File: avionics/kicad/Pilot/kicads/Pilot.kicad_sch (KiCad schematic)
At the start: 120 parts, among them X2Y-CAN 4.7nF X2Y, X2Y-RS485 4.7nF X2Y

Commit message: Pilot: move PB2 rails to 4.80 mm on male TSM-DV-LC strips and re-floor-plan (WBS R2)
The Pilot generator still had the unsourced 2.54 mm rail rows (29.92 mm
apart) and female socket footprints, so the cape could not mate with the
PB2-I. Same correction TACCO received on 2026-10-05:

- Rails at v 4.80 / 30.20 (PB2 SRM Fig. 3.45), Samtec TSM-118-04-L-DV-LC
  male SMT strips; -LC clip NPTHs at +/-20.32 mm.
- Bottom-face height budget (~5.54 mm stack, PB2-I microSD / JST-SH
  obstructions): both 8.9 mm Ethernet transformers to the top face, 1553
  transformer between the band and the JST-SH, GPS to B.Cu.
- TACCO-style isolation band: isolators on F.Cu at v 20.6, bus connectors
  at the bottom edge over the P2 rail, ISO_BAND on F.Cu + inner layers;
  only two-pad parts, GPS and 1553-XFM on B.Cu beneath it.
- J-PWM shifted 1.6 mm so its pad-1 column clears the P1 clip hole.

Gates: ERC 0 errors (10 accepted lib_symbol_issues), DRC 0 with schematic
parity 0, 120/120 placed, bottom-face height/under-band audit 0 violations.
Routing remains open.

Co-Authored-By: Claude Opus 5.5 <noreply@anthropic.com>
Claude-Session: https://claude.ai/code/session_01YLwDy53g1VCBzNBwW4moUC
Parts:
- PB2-P1: footprint Serenity-Custom:PocketBeagle2_2x18_P1_Socket -> Serenity-Custom:PocketBeagle2_2x18_P1_TSM-DV-LC; MPN (none) -> TSM-118-04-L-DV-LC
- PB2-P2: footprint Serenity-Custom:PocketBeagle2_2x18_P2_Socket -> Serenity-Custom:PocketBeagle2_2x18_P2_TSM-DV-LC; MPN (none) -> TSM-118-04-L-DV-LC
- TVS-CAN: footprint Package_TO_SOT_SMD:SOT-143 -> Package_TO_SOT_SMD:SOT-363_SC-70-6; symbol SecureControllers:PRTR5V0U2X -> Pilot:S_TVS-CAN
- TVS-RS485: footprint Package_TO_SOT_SMD:SOT-143 -> Package_TO_SOT_SMD:SOT-363_SC-70-6; symbol SecureControllers:PRTR5V0U2X -> Pilot:S_TVS-RS485
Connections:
- net CAN_H_F: now also TVS-CAN.1 (IO1); no longer TVS-CAN.2 (IO1)
- net GND2_CAN: now also TVS-CAN.2 (GND); no longer TVS-CAN.1 (GND)
- net GND2_RS485: now also TVS-RS485.2 (GND); no longer TVS-RS485.1 (GND)
- net RS485_A_F: now also TVS-RS485.1 (IO1); no longer TVS-RS485.2 (IO1)
- net VCC2_CAN: now also TVS-CAN.5 (VCC); no longer TVS-CAN.4 (VCC)
- net VCC2_RS485: now also TVS-RS485.5 (VCC); no longer TVS-RS485.4 (VCC)
- no-connect marks 87 -> 91
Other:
- note removed: "WÜRTH ELEKTRONIK USAGE NOTICE (verbatim, 749010012A data sheet rev 004.000 p.1; applies to Würth parts on this board: 749010012A, 742792512, WE-MAPI 3015): This electronic component has been designed and developed for usage in general electronic equipment only. This product is not authorized for use in equipment where a higher safety standard and reliability standard is especially required or whe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"

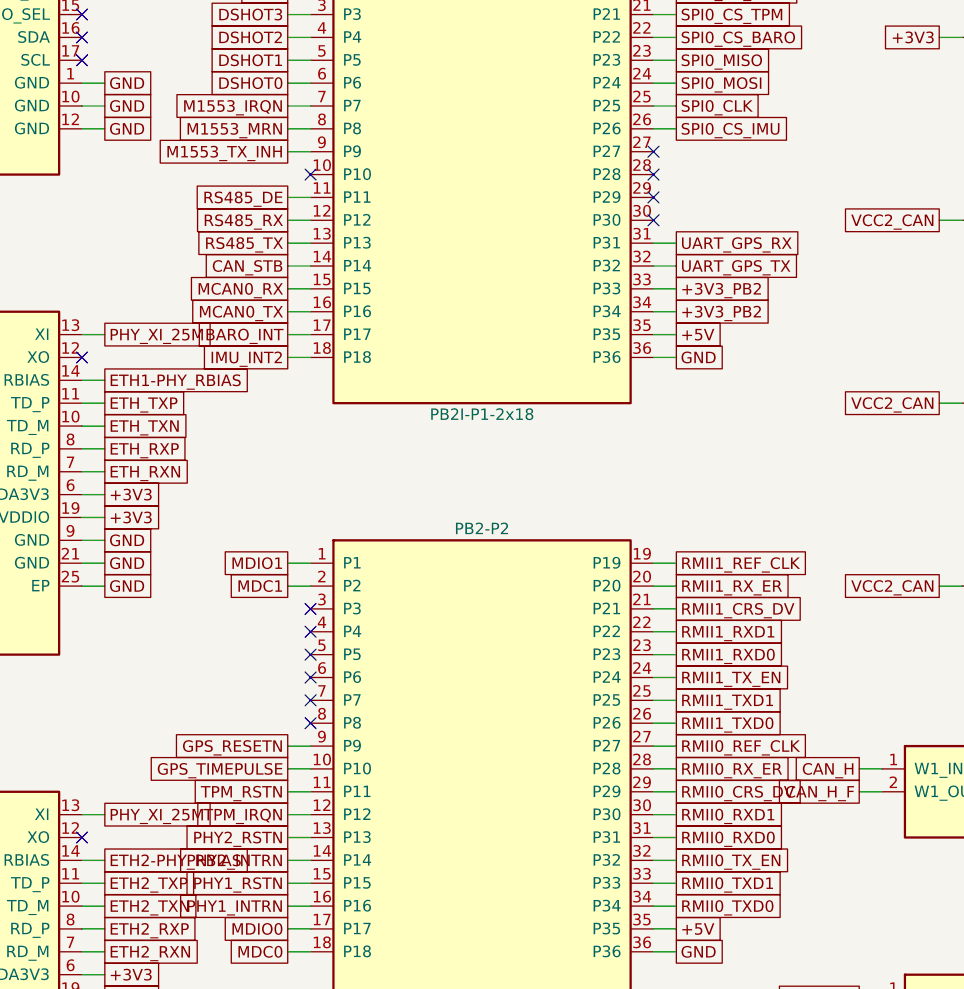
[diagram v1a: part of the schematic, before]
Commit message: Pilot: move TPM_RSTN/TPM_IRQN from PB2 P2-11/12 to P1-28/29 (ideation idea 10)
TPM sits over the P1 rail; P2-11/12 were 26-31 mm away and inside ISO_BAND
(no legal via). New pins P1-28 GPIO0_43 / P1-29 GPIO0_62 are 6-7 mm from TPM
pins 17/18, per PocketBeagle 2 SRM sec 4.2 mux tables. P1-27 (AIN4) and
P1-30 (UART0_TXD console) rejected.

- gen_pilot_sch.py pin map edited; generator verified byte-identical to the
  committed schematic before the edit; ERC 0 before and after.
- Pilot.net re-exported; PCB pad nets edited in place (owner hand placement
  preserved): DRC 0 errors, parity 0, 136 unconnected (unchanged; both nets
  were already unrouted, now short).
- Idea 11 (clock HI-6138 from PHY 50MHzOut, delete X-50M) NOT done: contradicts
  the recorded decision that a PHY reset must not stop 1553, and needs a
  22-23 mm 50 MHz branch vs the current 1.6 mm oscillator trace.

Co-Authored-By: Claude Opus 5.5 (1M context) <noreply@anthropic.com>
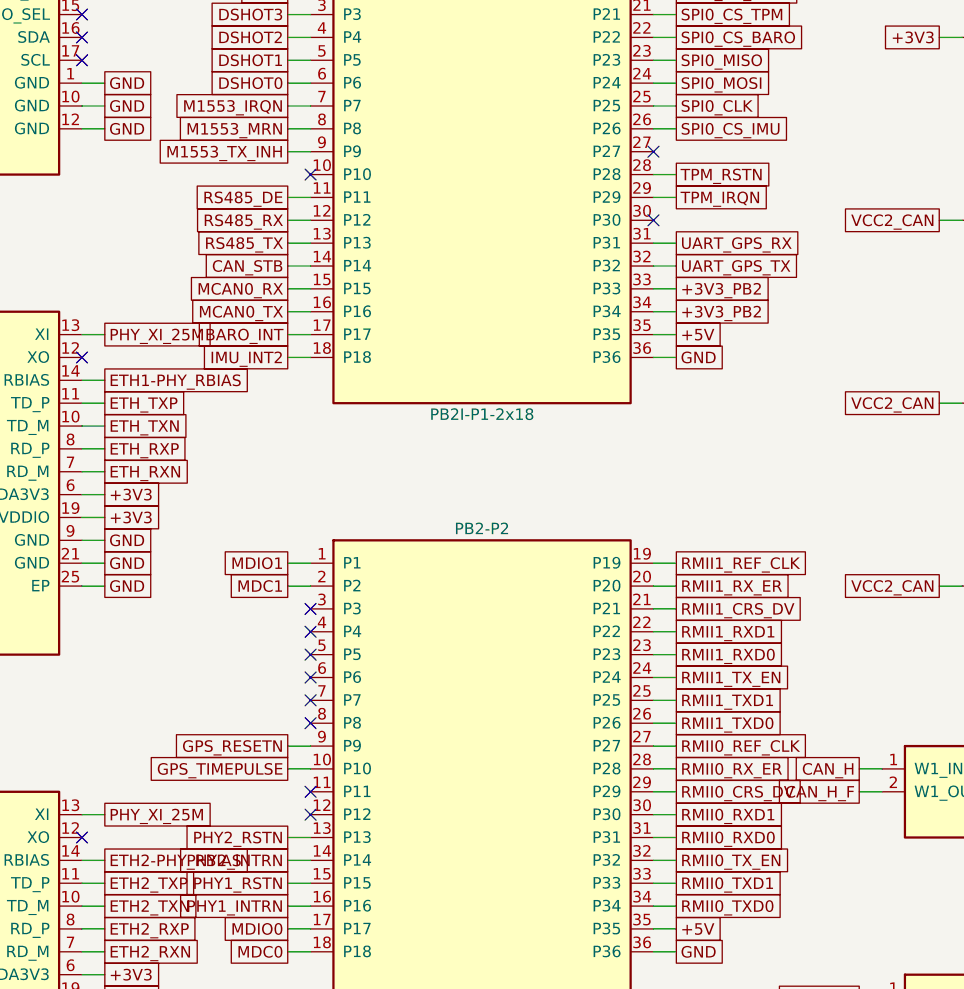
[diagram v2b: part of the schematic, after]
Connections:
- net TPM_IRQN: now also PB2-P1.29 (P29); no longer PB2-P2.12 (P12)
- net TPM_RSTN: now also PB2-P1.28 (P28); no longer PB2-P2.11 (P11)
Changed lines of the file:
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@@
   (global_label "SPI0_CS_IMU" (shape passive) (at 161.29 271.78 0) (effects (font (size 1.27 1.27)) (justify left)))
   (no_connect (at 158.75 274.32))
-  (no_connect (at 158.75 276.86))
-  (no_connect (at 158.75 279.40))
+  (wire (pts (xy 158.75 276.86) (xy 161.29 276.86)) (stroke (width 0) (type default)))
+  (global_label "TPM_RSTN" (shape passive) (at 161.29 276.86 0) (effects (font (size 1.27 1.27)) (justify left)))
+  (wire (pts (xy 158.75 279.40) (xy 161.29 279.40)) (stroke (width 0) (type default)))
+  (global_label "TPM_IRQN" (shape passive) (at 161.29 279.40 0) (effects (font (size 1.27 1.27)) (justify left)))
   (no_connect (at 158.75 281.94))
   (wire (pts (xy 158.75 284.48) (xy 161.29 284.48)) (stroke (width 0) (type default)))
@@
   (wire (pts (xy 120.65 342.90) (xy 118.11 342.90)) (stroke (width 0) (type default)))
   (global_label "GPS_TIMEPULSE" (shape passive) (at 118.11 342.90 180) (effects (font (size 1.27 1.27)) (justify right)))
-  (wire (pts (xy 120.65 345.44) (xy 118.11 345.44)) (stroke (width 0) (type default)))
-  (global_label "TPM_RSTN" (shape passive) (at 118.11 345.44 180) (effects (font (size 1.27 1.27)) (justify right)))
-  (wire (pts (xy 120.65 347.98) (xy 118.11 347.98)) (stroke (width 0) (type default)))
-  (global_label "TPM_IRQN" (shape passive) (at 118.11 347.98 180) (effects (font (size 1.27 1.27)) (justify right)))
+  (no_connect (at 120.65 345.44))
+  (no_connect (at 120.65 347.98))
   (wire (pts (xy 120.65 350.52) (xy 118.11 350.52)) (stroke (width 0) (type default)))
   (global_label "PHY2_RSTN" (shape passive) (at 118.11 350.52 180) (effects (font (size 1.27 1.27)) (justify right)))

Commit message: Pilot sch: ISOW §13.1 ferrite beads + split DC-DC output nets (ERC 0)
Owner decision 2026-10-12: treat ISOW1044 SLLSFF7A §13.1 [REF-SENSOR-009] and
ISOW1412 SLLSF86C §13.1 [REF-SENSOR-010] as binding.

- New nets VCC2_CAN_DCDC / GND2_CAN_DCDC / VCC2_RS485_DCDC / GND2_RS485_DCDC
  on VISOOUT (12, + VSIN 13 on ISOW1044) and GND2 (11); ISOW1412 MODE (13)
  tied to GND2 per §13.1.
- Four BLM15EX331SN1D beads (FB-CAN-V/G, FB-485-V/G) between VISOOUT->VISOIN
  and GND2->GISOIN (§13.1 item 4) [REF-SENSOR-043, new].
- C-CAN4 / C-485-4 10 nF HF caps 0201 -> 0402 on the DC-DC side (item 2);
  bulk C-CAN5 / C-485-5 on the DC-DC side (item 3).
- 124 parts, 599 pins, ERC 0; netlist re-exported.  PCB not yet updated.

Co-Authored-By: Claude Opus 5.5 (1M context) <noreply@anthropic.com>
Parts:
- removed C-1553A: 100nF, Capacitor_SMD:C_0402_1005Metric, symbol Pilot:S_C-1553A
- removed C-1553B: 100nF, Capacitor_SMD:C_0402_1005Metric, symbol Pilot:S_C-1553B
- removed C-25M: 100nF, Capacitor_SMD:C_0402_1005Metric, symbol Pilot:S_C-25M
- removed C-485-1: 10nF, Capacitor_SMD:C_0201_0603Metric, symbol Pilot:S_C-485-1
- removed C-485-2: 10uF 10V X5R, Capacitor_SMD:C_0805_2012Metric, symbol Pilot:S_C-485-2
- removed C-50M: 100nF, Capacitor_SMD:C_0402_1005Metric, symbol Pilot:S_C-50M
- removed C-BARO1: 100nF, Capacitor_SMD:C_0402_1005Metric, symbol Pilot:S_C-BARO1
- removed C-BS1: 10nF 2kV, Capacitor_SMD:C_1808_4520Metric, symbol Pilot:S_C-BS1
- removed C-IMU1: 100nF, Capacitor_SMD:C_0402_1005Metric, symbol Pilot:S_C-IMU1
- removed C-IMU2: 10nF, Capacitor_SMD:C_0201_0603Metric, symbol Pilot:S_C-IMU2
- removed C-P1-A1: 10nF, Capacitor_SMD:C_0201_0603Metric, symbol Pilot:S_C-P1-A1
- removed C-P1-A2: 100nF, Capacitor_SMD:C_0402_1005Metric, symbol Pilot:S_C-P1-A2
- removed R-1553P: 55R 2%, Resistor_SMD:R_0603_1608Metric, symbol Pilot:S_R-1553P
- removed R-BS1R: 75R, Resistor_SMD:R_0402_1005Metric, symbol Pilot:S_R-BS1R
- removed R-BS1T: 75R, Resistor_SMD:R_0402_1005Metric, symbol Pilot:S_R-BS1T
- removed R-P1-AD0: 2.49k, Resistor_SMD:R_0201_0603Metric, symbol Pilot:S_R-P1-AD0
- removed R-P1-RBIAS: 6.49k 1%, Resistor_SMD:R_0201_0603Metric, symbol Pilot:S_R-P1-RBIAS
- added C-485-6: 100nF, Capacitor_SMD:C_0402_1005Metric, symbol Pilot:S_C-485-6
- added C-BS2: 10nF 2kV, Capacitor_SMD:C_1808_4520Metric, symbol Pilot:S_C-BS2
- added C-CAN6: 100nF, Capacitor_SMD:C_0402_1005Metric, symbol Pilot:S_C-CAN6
- added C-P2-CRD1: 100nF, Capacitor_SMD:C_0402_1005Metric, symbol Pilot:S_C-P2-CRD1
- added C-P2-CRD2: 1uF, Capacitor_SMD:C_0402_1005Metric, symbol Pilot:S_C-P2-CRD2
- added C-P2-CTD1: 100nF, Capacitor_SMD:C_0402_1005Metric, symbol Pilot:S_C-P2-CTD1
- added C-P2-CTD2: 1uF, Capacitor_SMD:C_0402_1005Metric, symbol Pilot:S_C-P2-CTD2
- added C-TPM4: 100nF, Capacitor_SMD:C_0402_1005Metric, symbol Pilot:S_C-TPM4
- added CMC-CAN: SRF2012-100Y, Serenity-Custom:Bourns_SRF2012_4T, symbol Pilot:S_CMC-CAN
- added CMC-RS485: SRF2012-100Y, Serenity-Custom:Bourns_SRF2012_4T, symbol Pilot:S_CMC-RS485
- added FB-485-G: 330R@100MHz, Inductor_SMD:L_0402_1005Metric, symbol Pilot:S_FB-485-G
- added FB-485-V: 330R@100MHz, Inductor_SMD:L_0402_1005Metric, symbol Pilot:S_FB-485-V
- added J-PWM: TSM-108-01-L-DV, Serenity-Custom:Samtec_TSM-108-01-x-DV, symbol Pilot:S_J-PWM
- added MIL-1553: SM04B-GHS-TB, Connector_JST:JST_GH_SM04B-GHS-TB_1x04-1MP_P1.25mm_Horizontal, symbol Pilot:S_MIL-1553
- added R-1553IRQ: 10k, Resistor_SMD:R_0402_1005Metric, symbol Pilot:S_R-1553IRQ
- added R-BS2R: 75R, Resistor_SMD:R_0402_1005Metric, symbol Pilot:S_R-BS2R
- added R-TPM10: 10k, Resistor_SMD:R_0201_0603Metric, symbol Pilot:S_R-TPM10
- added R-TPMCS: 10k, Resistor_SMD:R_0201_0603Metric, symbol Pilot:S_R-TPMCS
- added TVS-1553N: SMAJ33CA, Diode_SMD:D_SMA, symbol Pilot:S_TVS-1553N
- added X-25M: 25MHz 3.3V, Oscillator:Oscillator_SMD_ECS_2520MV-xxx-xx-4Pin_2.5x2.0mm, symbol Pilot:S_X-25M
- added X-50M: 50MHz 3.3V, Oscillator:Oscillator_SMD_ECS_2520MV-xxx-xx-4Pin_2.5x2.0mm, symbol Pilot:S_X-50M
- C-1553A: renamed from R-1553IRQ; value 10k -> 100nF; footprint Resistor_SMD:R_0402_1005Metric -> Capacitor_SMD:C_0402_1005Metric; symbol Pilot:S_R-1553IRQ -> Pilot:S_C-1553A
- C-1553B: renamed from X-50M; value 50MHz 3.3V -> 100nF; footprint Oscillator:Oscillator_SMD_ECS_2520MV-xxx-xx-4Pin_2.5x2.0mm -> Capacitor_SMD:C_0402_1005Metric; symbol Pilot:S_X-50M -> Pilot:S_C-1553B; MPN ECS-2520MV-500-BN-TR -> (none)
- C-25M: renamed from TVS-1553N; value SMAJ33CA -> 100nF; footprint Diode_SMD:D_SMA -> Capacitor_SMD:C_0402_1005Metric; symbol Pilot:S_TVS-1553N -> Pilot:S_C-25M; MPN SMAJ33CA -> (none)
- C-485-1: renamed from C-485-3; value 100nF -> 10nF; footprint Capacitor_SMD:C_0402_1005Metric -> Capacitor_SMD:C_0201_0603Metric; symbol Pilot:S_C-485-3 -> Pilot:S_C-485-1
- C-485-2: renamed from C-485-4; value 10nF -> 10uF 10V X5R; footprint Capacitor_SMD:C_0201_0603Metric -> Capacitor_SMD:C_0805_2012Metric; symbol Pilot:S_C-485-4 -> Pilot:S_C-485-2
- C-485-3: renamed from C-485-5; value 10uF 10V X5R -> 100nF; footprint Capacitor_SMD:C_0805_2012Metric -> Capacitor_SMD:C_0402_1005Metric; symbol Pilot:S_C-485-5 -> Pilot:S_C-485-3
- C-485-4: renamed from C-485-6; value 100nF -> 10nF; symbol Pilot:S_C-485-6 -> Pilot:S_C-485-4
- C-485-5: renamed from CMC-RS485; value SRF2012-100Y -> 10uF 10V X5R; footprint Serenity-Custom:Bourns_SRF2012_4T -> Capacitor_SMD:C_0805_2012Metric; symbol Pilot:S_CMC-RS485 -> Pilot:S_C-485-5; MPN SRF2012-121YA -> (none)
- C-50M: renamed from C-BARO2; symbol Pilot:S_C-BARO2 -> Pilot:S_C-50M
- C-ANT: renamed from C-TPM2; value 100nF -> 10nF X7R; symbol Pilot:S_C-TPM2 -> Pilot:S_C-ANT
- C-BARO1: renamed from R-ANT; value 10R -> 100nF; footprint Resistor_SMD:R_0201_0603Metric -> Capacitor_SMD:C_0402_1005Metric; symbol Pilot:S_R-ANT -> Pilot:S_C-BARO1
- C-BARO2: renamed from C-ANT; value 10nF X7R -> 100nF; symbol Pilot:S_C-ANT -> Pilot:S_C-BARO2
- C-BS1: renamed from X-25M; value 25MHz 3.3V -> 10nF 2kV; footprint Oscillator:Oscillator_SMD_ECS_2520MV-xxx-xx-4Pin_2.5x2.0mm -> Capacitor_SMD:C_1808_4520Metric; symbol Pilot:S_X-25M -> Pilot:S_C-BS1; MPN ECS-2520MV-250-BN-TR -> (none)
- C-CAN4: footprint Capacitor_SMD:C_0201_0603Metric -> Capacitor_SMD:C_0402_1005Metric
- C-GPS1: renamed from L-ANT; value 27nH -> 10uF 6.3V X5R; footprint Inductor_SMD:L_0402_1005Metric -> Capacitor_SMD:C_0805_2012Metric; symbol Pilot:S_L-ANT -> Pilot:S_C-GPS1; MPN LQG15HN27NJ02D -> (none)
- C-GPS2: renamed from J-ANT; value U.FL-R-SMT-1 -> 100nF; footprint Connector_Coaxial:U.FL_Hirose_U.FL-R-SMT-1_Vertical -> Capacitor_SMD:C_0402_1005Metric; symbol Pilot:S_J-ANT -> Pilot:S_C-GPS2; MPN U.FL-R-SMT-1(10) -> (none)
- C-IMU1: renamed from C-GPS1; value 10uF 6.3V X5R -> 100nF; footprint Capacitor_SMD:C_0805_2012Metric -> Capacitor_SMD:C_0402_1005Metric; symbol Pilot:S_C-GPS1 -> Pilot:S_C-IMU1
- C-IMU2: renamed from C-GPS2; value 100nF -> 10nF; footprint Capacitor_SMD:C_0402_1005Metric -> Capacitor_SMD:C_0201_0603Metric; symbol Pilot:S_C-GPS2 -> Pilot:S_C-IMU2
- C-P1-A1: renamed from C-P1-IO2; value 100nF -> 10nF; footprint Capacitor_SMD:C_0402_1005Metric -> Capacitor_SMD:C_0201_0603Metric; symbol Pilot:S_C-P1-IO2 -> Pilot:S_C-P1-A1
- C-P1-A2: renamed from C-P1-IO3; value 1uF -> 100nF; symbol Pilot:S_C-P1-IO3 -> Pilot:S_C-P1-A2
- C-P1-A3: renamed from C-P1-CTD1; value 100nF -> 1uF; symbol Pilot:S_C-P1-CTD1 -> Pilot:S_C-P1-A3
- C-P1-CRD1: renamed from C-P2-A1; value 10nF -> 100nF; footprint Capacitor_SMD:C_0201_0603Metric -> Capacitor_SMD:C_0402_1005Metric; symbol Pilot:S_C-P2-A1 -> Pilot:S_C-P1-CRD1
- C-P1-CRD2: renamed from C-P2-A2; value 100nF -> 1uF; symbol Pilot:S_C-P2-A2 -> Pilot:S_C-P1-CRD2
- C-P1-CTD1: renamed from R-P2-RBIAS; value 6.49k 1% -> 100nF; footprint Resistor_SMD:R_0201_0603Metric -> Capacitor_SMD:C_0402_1005Metric; symbol Pilot:S_R-P2-RBIAS -> Pilot:S_C-P1-CTD1
- C-P1-CTD2: renamed from R-P2-AD0; value 2.49k -> 1uF; footprint Resistor_SMD:R_0201_0603Metric -> Capacitor_SMD:C_0402_1005Metric; symbol Pilot:S_R-P2-AD0 -> Pilot:S_C-P1-CTD2
- C-P1-IO1: renamed from C-P1-CTD2; value 1uF -> 10nF; footprint Capacitor_SMD:C_0402_1005Metric -> Capacitor_SMD:C_0201_0603Metric; symbol Pilot:S_C-P1-CTD2 -> Pilot:S_C-P1-IO1
- C-P1-IO2: renamed from C-P1-CRD1; symbol Pilot:S_C-P1-CRD1 -> Pilot:S_C-P1-IO2
- C-P1-IO3: renamed from C-P1-CRD2; symbol Pilot:S_C-P1-CRD2 -> Pilot:S_C-P1-IO3
- C-P2-A1: renamed from C-P2-IO2; value 100nF -> 10nF; footprint Capacitor_SMD:C_0402_1005Metric -> Capacitor_SMD:C_0201_0603Metric; symbol Pilot:S_C-P2-IO2 -> Pilot:S_C-P2-A1
- C-P2-A2: renamed from C-P2-IO3; value 1uF -> 100nF; symbol Pilot:S_C-P2-IO3 -> Pilot:S_C-P2-A2
- C-P2-A3: renamed from C-P2-CTD1; value 100nF -> 1uF; symbol Pilot:S_C-P2-CTD1 -> Pilot:S_C-P2-A3
- C-P2-IO1: renamed from C-P2-CTD2; value 1uF -> 10nF; footprint Capacitor_SMD:C_0402_1005Metric -> Capacitor_SMD:C_0201_0603Metric; symbol Pilot:S_C-P2-CTD2 -> Pilot:S_C-P2-IO1
- C-P2-IO2: renamed from C-P2-CRD1; symbol Pilot:S_C-P2-CRD1 -> Pilot:S_C-P2-IO2
- C-P2-IO3: renamed from C-P2-CRD2; symbol Pilot:S_C-P2-CRD2 -> Pilot:S_C-P2-IO3
- C-TPM1: renamed from R-TPMCS; value 10k -> 1uF; footprint Resistor_SMD:R_0201_0603Metric -> Capacitor_SMD:C_0402_1005Metric; symbol Pilot:S_R-TPMCS -> Pilot:S_C-TPM1
- C-TPM2: renamed from R-TPM10; value 10k -> 100nF; footprint Resistor_SMD:R_0201_0603Metric -> Capacitor_SMD:C_0402_1005Metric; symbol Pilot:S_R-TPM10 -> Pilot:S_C-TPM2
- C-TPM3: renamed from J-PWM; value TSM-108-01-L-DV -> 100nF; footprint Serenity-Custom:Samtec_TSM-108-01-x-DV -> Capacitor_SMD:C_0402_1005Metric; symbol Pilot:S_J-PWM -> Pilot:S_C-TPM3; MPN TSM-108-01-L-DV -> (none)
- FB-CAN-G: renamed from CMC-CAN; value SRF2012-100Y -> 330R@100MHz; footprint Serenity-Custom:Bourns_SRF2012_4T -> Inductor_SMD:L_0402_1005Metric; symbol Pilot:S_CMC-CAN -> Pilot:S_FB-CAN-G; MPN SRF2012-121YA -> BLM15EX331SN1D
- FB-CAN-V: renamed from C-CAN6; value 100nF -> 330R@100MHz; footprint Capacitor_SMD:C_0402_1005Metric -> Inductor_SMD:L_0402_1005Metric; symbol Pilot:S_C-CAN6 -> Pilot:S_FB-CAN-V; MPN (none) -> BLM15EX331SN1D
- J-ANT: renamed from C-TPM4; value 100nF -> U.FL-R-SMT-1; footprint Capacitor_SMD:C_0402_1005Metric -> Connector_Coaxial:U.FL_Hirose_U.FL-R-SMT-1_Vertical; symbol Pilot:S_C-TPM4 -> Pilot:S_J-ANT; MPN (none) -> U.FL-R-SMT-1(10)
- L-ANT: renamed from C-TPM3; value 100nF -> 27nH; footprint Capacitor_SMD:C_0402_1005Metric -> Inductor_SMD:L_0402_1005Metric; symbol Pilot:S_C-TPM3 -> Pilot:S_L-ANT; MPN (none) -> LQG15HN27NJ02D
- R-1553P: renamed from MIL-1553; value SM04B-GHS-TB -> 55R 2%; footprint Connector_JST:JST_GH_SM04B-GHS-TB_1x04-1MP_P1.25mm_Horizontal -> Resistor_SMD:R_0603_1608Metric; symbol Pilot:S_MIL-1553 -> Pilot:S_R-1553P; MPN SM04B-GHS-TB(LF)(SN) -> (none)
- R-ANT: renamed from C-TPM1; value 1uF -> 10R; footprint Capacitor_SMD:C_0402_1005Metric -> Resistor_SMD:R_0201_0603Metric; symbol Pilot:S_C-TPM1 -> Pilot:S_R-ANT
- R-BS1R: renamed from C-BS2; value 10nF 2kV -> 75R; footprint Capacitor_SMD:C_1808_4520Metric -> Resistor_SMD:R_0402_1005Metric; symbol Pilot:S_C-BS2 -> Pilot:S_R-BS1R
- R-BS1T: renamed from R-BS2R; symbol Pilot:S_R-BS2R -> Pilot:S_R-BS1T
- R-P1-AD0: renamed from C-P1-IO1; value 10nF -> 2.49k; footprint Capacitor_SMD:C_0201_0603Metric -> Resistor_SMD:R_0201_0603Metric; symbol Pilot:S_C-P1-IO1 -> Pilot:S_R-P1-AD0
- R-P1-RBIAS: renamed from C-P1-A3; value 1uF -> 6.49k 1%; footprint Capacitor_SMD:C_0402_1005Metric -> Resistor_SMD:R_0201_0603Metric; symbol Pilot:S_C-P1-A3 -> Pilot:S_R-P1-RBIAS
- R-P2-AD0: renamed from C-P2-IO1; value 10nF -> 2.49k; footprint Capacitor_SMD:C_0201_0603Metric -> Resistor_SMD:R_0201_0603Metric; symbol Pilot:S_C-P2-IO1 -> Pilot:S_R-P2-AD0
- R-P2-RBIAS: renamed from C-P2-A3; value 1uF -> 6.49k 1%; footprint Capacitor_SMD:C_0402_1005Metric -> Resistor_SMD:R_0201_0603Metric; symbol Pilot:S_C-P2-A3 -> Pilot:S_R-P2-RBIAS
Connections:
- net +3V3: now also C-1553B.1 (P), C-25M.1 (P), C-485-3.1 (P), C-BARO1.1 (P), C-BARO2.1 (P), C-GPS1.1 (P), C-GPS2.1 (P), C-P1-A3.1 (P), C-P1-IO1.1 (P), C-P1-IO2.1 (P), C-P1-IO3.1 (P), C-P2-A3.1 (P), C-P2-IO1.1 (P), C-P2-IO2.1 (P), C-P2-IO3.1 (P), C-TPM3.1 (P), C-TPM4.1 (P), R-1553IRQ.1 (A), R-TPM10.1 (A), R-TPMCS.1 (A), X-25M.4 (VDD), X-50M.4 (VDD); no longer C-1553B.4 (VDD), C-485-1.1 (P), C-ANT.1 (P), C-BS1.4 (VDD), C-P1-CRD1.1 (P), C-P1-CRD2.1 (P), C-P1-CTD2.1 (A), J-ANT.1 (P), L-ANT.1 (P), R-ANT.1 (P), R-P1-RBIAS.1 (P), R-P2-RBIAS.1 (P)
- net +5V: now also C-485-1.1 (P), C-485-2.1 (P), J-PWM.11 (+5V_1), J-PWM.12 (+5V_3), J-PWM.3 (+5V_0), J-PWM.4 (+5V_2); no longer C-TPM3.11 (+5V_1), C-TPM3.12 (+5V_3), C-TPM3.3 (+5V_0), C-TPM3.4 (+5V_2)
- net BUS_1553_N: now also MIL-1553.2 (BUS_N), TVS-1553N.1 (A); no longer C-25M.1 (A), R-1553P.2 (BUS_N)
- net BUS_1553_P: now also R-1553P.2 (B), MIL-1553.1 (BUS_P); no longer R-1553P.1 (BUS_P)
- net CAN_H: now also CMC-CAN.1 (W1_IN); no longer FB-CAN-G.1 (W1_IN)
- net CAN_H_F: now also CMC-CAN.2 (W1_OUT); no longer FB-CAN-G.2 (W1_OUT)
- net CAN_L: now also CMC-CAN.4 (W2_IN); no longer FB-CAN-G.4 (W2_IN)
- net CAN_L_F: now also CMC-CAN.3 (W2_OUT); no longer FB-CAN-G.3 (W2_OUT)
- net DSHOT0: now also J-PWM.1 (SIG0); no longer C-TPM3.1 (SIG0)
- net DSHOT1: now also J-PWM.9 (SIG1); no longer C-TPM3.9 (SIG1)
- net DSHOT2: now also J-PWM.2 (SIG2); no longer C-TPM3.2 (SIG2)
- net DSHOT3: now also J-PWM.10 (SIG3); no longer C-TPM3.10 (SIG3)
- net ETH1-PHY_RBIAS: now also R-P1-RBIAS.1 (A)
- net ETH2-PHY_RBIAS: now also R-P2-RBIAS.1 (A); no longer C-P1-CTD1.1 (A)
- net ETH2_BS: now also C-BS2.1 (P), R-BS2R.2 (B); no longer R-BS1R.1 (P), R-BS1T.2 (B)
- net ETH2_CRD: now also C-P2-CRD1.1 (P), C-P2-CRD2.1 (P); no longer C-P2-IO2.1 (P), C-P2-IO3.1 (P)
- net ETH2_CTD: now also C-P2-CTD1.1 (P), C-P2-CTD2.1 (P); no longer C-P2-A3.1 (P), C-P2-IO1.1 (P)
- net ETH2_LINE_CRX: now also R-BS2R.1 (A); no longer R-BS1T.1 (A)
- net ETH_BS: now also C-BS1.1 (P), R-BS1R.2 (B), R-BS1T.2 (B)
- net ETH_CRD: now also C-P1-CRD1.1 (P), C-P1-CRD2.1 (P); no longer C-P1-IO2.1 (P), C-P1-IO3.1 (P)
- net ETH_CTD: now also C-P1-CTD1.1 (P), C-P1-CTD2.1 (P); no longer C-P1-A3.1 (P), C-P1-IO1.1 (P)
- net ETH_LINE_CRX: now also R-BS1R.1 (A)
- net ETH_LINE_CTX: now also R-BS1T.1 (A)
- net GND: now also C-1553A.2 (N), C-25M.2 (N), C-485-2.2 (N), C-485-3.2 (N), C-BARO1.2 (N), C-GPS1.2 (N), C-P1-CTD2.2 (N), C-TPM1.2 (N), C-TPM2.2 (N), C-TPM3.2 (N), C-P2-CRD1.2 (N), C-P2-CRD2.2 (N), C-P2-CTD1.2 (N), C-P2-CTD2.2 (N), C-TPM4.2 (N), J-PWM.13 (GND1), J-PWM.14 (GND3), J-PWM.5 (GND0), J-PWM.6 (GND2), MIL-1553.3 (GND), X-25M.2 (GND), X-50M.2 (GND); no longer C-BS1.2 (GND), C-TPM3.13 (GND1), C-TPM3.14 (GND3), C-TPM3.5 (GND0), C-TPM3.6 (GND2), L-ANT.2 (N), R-1553P.3 (GND), R-ANT.2 (N), R-P1-AD0.2 (N), R-P2-AD0.2 (N)
- net GND2_CAN: now also FB-CAN-G.2 (B), C-CAN6.2 (N); no longer C-CAN4.2 (N), C-CAN5.2 (N), CAN-TR.11 (GND2), FB-CAN-V.2 (N)
- net GND2_RS485: now also C-485-6.2 (N), FB-485-G.2 (B); no longer C-485-2.2 (N), C-485-3.2 (N), C-485-4.2 (N), RS485.11 (GND2), RS485.13 (MODE)
- net GPS_ANT_BIAS: now also C-ANT.1 (P), L-ANT.1 (A), R-ANT.2 (B); no longer C-BARO1.2 (B), C-BARO2.1 (P), C-GPS1.1 (A)
- net GPS_RF: now also J-ANT.1 (RF), L-ANT.2 (B); no longer C-GPS1.2 (B), C-GPS2.1 (RF)
- net GPS_VCC_RF: now also R-ANT.1 (A); no longer C-BARO1.1 (A)
- net M1553_IRQN: now also R-1553IRQ.2 (B); no longer C-1553A.2 (B)
- net M1553_MCLK: now also X-50M.3 (OUT); no longer C-1553B.3 (OUT)
- net M1553_SEC_P: now also R-1553P.1 (A)
- net PGND: now also C-BS1.2 (N), C-BS2.2 (N), J-PWM.15 (SHLD1), J-PWM.16 (SHLD3), J-PWM.7 (SHLD0), J-PWM.8 (SHLD2), MIL-1553.4 (SHIELD), MIL-1553.MP (SHIELD), TVS-1553N.2 (K); no longer C-25M.2 (K), C-TPM3.15 (SHLD1), C-TPM3.16 (SHLD3), C-TPM3.7 (SHLD0), C-TPM3.8 (SHLD2), R-1553P.4 (SHIELD), R-1553P.MP (SHIELD), R-BS1R.2 (N)
- net PHY_XI_25M: now also X-25M.3 (OUT); no longer C-BS1.3 (OUT)
- net RMII0_RXD0: now also R-P1-AD0.2 (B)
- net RMII1_RXD0: now also R-P2-AD0.2 (B); no longer C-P1-CTD2.2 (B)
- net RS485_A: now also CMC-RS485.1 (W1_IN); no longer C-485-5.1 (W1_IN)
- net RS485_A_F: now also CMC-RS485.2 (W1_OUT); no longer C-485-5.2 (W1_OUT)
- net RS485_B: now also CMC-RS485.4 (W2_IN); no longer C-485-5.4 (W2_IN)
- net RS485_B_F: now also CMC-RS485.3 (W2_OUT); no longer C-485-5.3 (W2_OUT)
- net SPI0_CS_TPM: now also R-TPMCS.2 (B); no longer C-TPM1.2 (B)
- net TPM_P10_PU: now also R-TPM10.2 (B); no longer C-TPM2.2 (B)
- net VCC2_CAN: now also FB-CAN-V.2 (B), C-CAN6.1 (P); no longer C-CAN4.1 (P), C-CAN5.1 (P), CAN-TR.12 (VISOOUT), CAN-TR.13 (VSIN), FB-CAN-V.1 (P)
- net VCC2_RS485: now also C-485-6.1 (P), FB-485-V.2 (B); no longer C-485-2.1 (P), C-485-3.1 (P), C-485-4.1 (P), RS485.12 (VISOOUT)
- new net GND2_CAN_DCDC: C-CAN4.2 (N), C-CAN5.2 (N), CAN-TR.11 (GND2), FB-CAN-G.1 (A)
- new net GND2_RS485_DCDC: C-485-4.2 (N), C-485-5.2 (N), FB-485-G.1 (A), RS485.11 (GND2), RS485.13 (MODE)
- new net VCC2_CAN_DCDC: C-CAN4.1 (P), C-CAN5.1 (P), CAN-TR.12 (VISOOUT), CAN-TR.13 (VSIN), FB-CAN-V.1 (A)
- new net VCC2_RS485_DCDC: C-485-4.1 (P), C-485-5.1 (P), FB-485-V.1 (A), RS485.12 (VISOOUT)
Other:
- moved on the sheet: C-1553A, C-50M, C-ANT, C-BARO1, C-BARO2, C-GPS1, C-GPS2, C-IMU1, C-IMU2, C-P1-A1, C-P1-A2, C-P1-A3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
